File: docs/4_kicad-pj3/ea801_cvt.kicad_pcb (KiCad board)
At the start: 2 copper layers, 4 parts, among them J99 PinHeader_1x02_P2.54mm_Vertic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

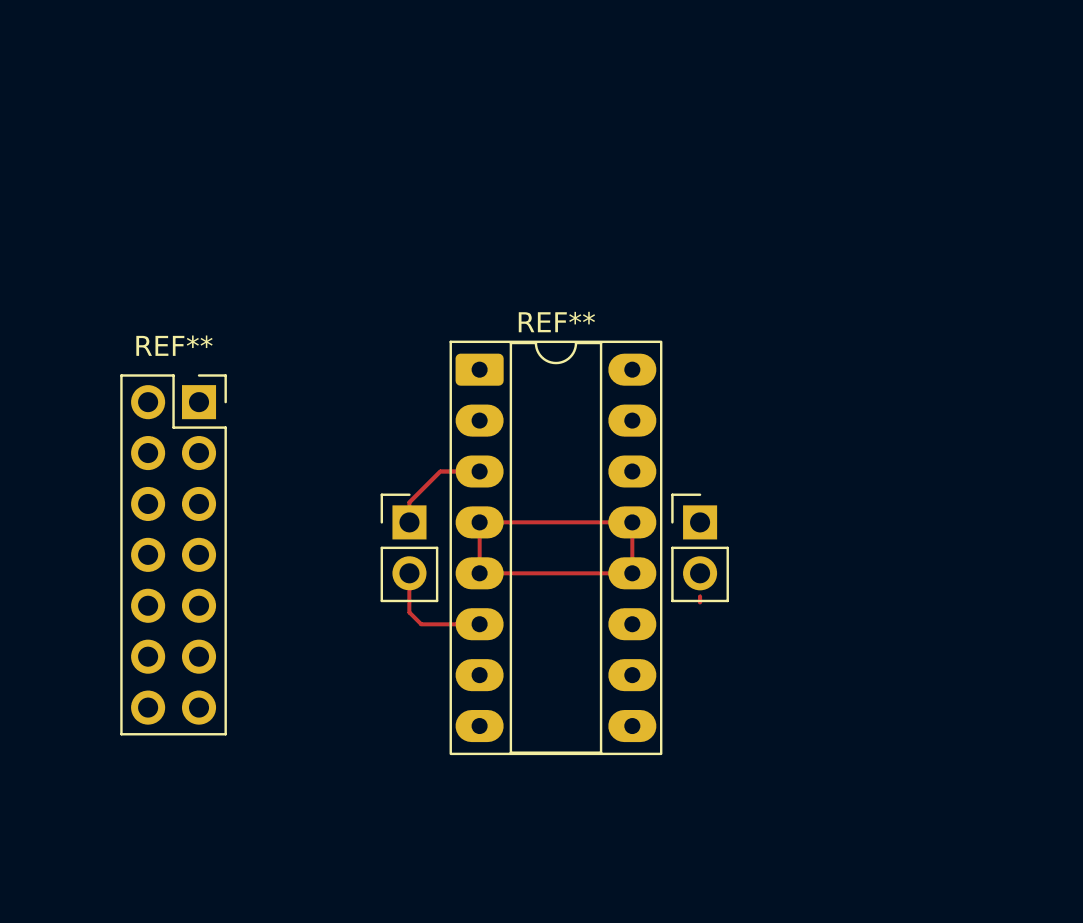
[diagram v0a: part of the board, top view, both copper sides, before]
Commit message: inc imagens, att projeto kicad e att dos arquivos do sensor ToF
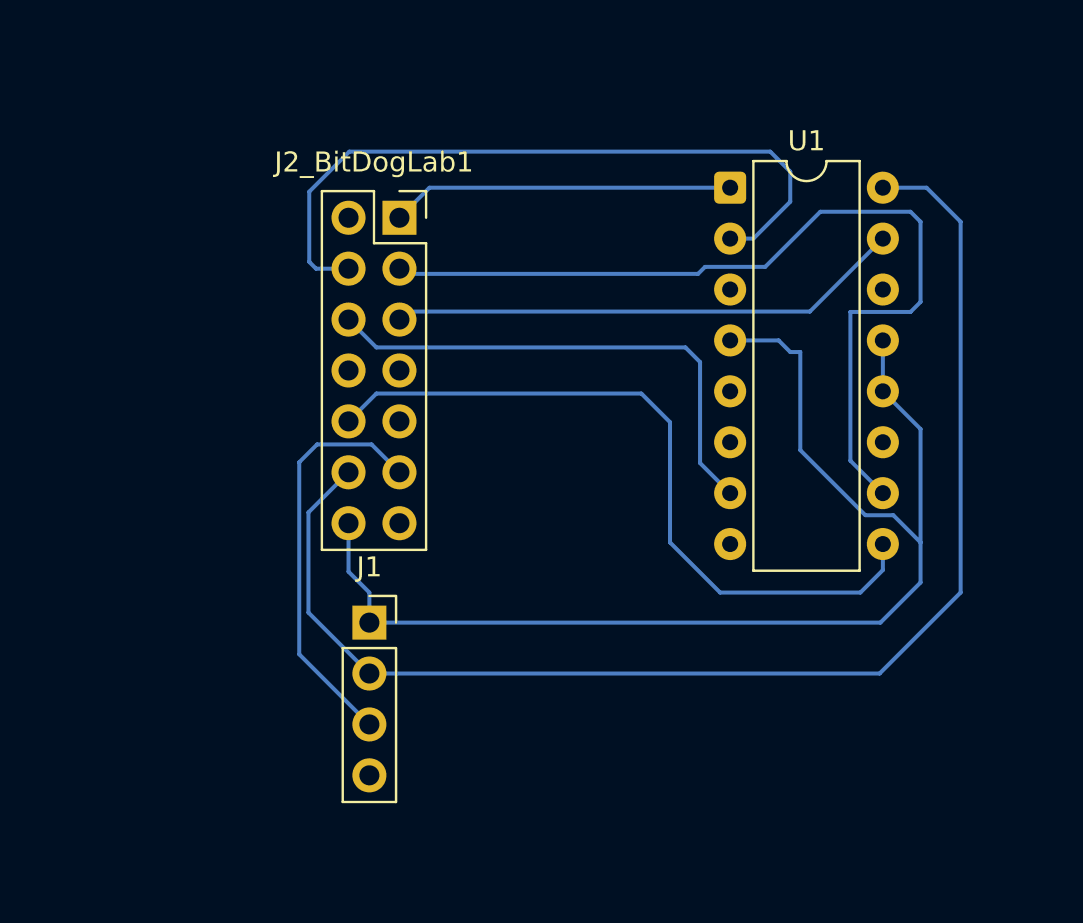
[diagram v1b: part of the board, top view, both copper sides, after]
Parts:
- removed J99, REF**: PinHeader_1x02_P2.54mm_Vertical, Connector_PinHeader_2.54mm:PinHeader_1x02_P2.54mm_Vertical
- removed REF**: CERDIP-16_W7.62mm_SideBrazed_LongPads_Socket, Package_DIP:CERDIP-16_W7.62mm_SideBrazed_LongPads_Socket
- removed REF**: PinSocket_2x07_P2.54mm_Vertical, Connector_PinSocket_2.54mm:PinSocket_2x07_P2.54mm_Vertical
- added J1: Conn_01x04, Connector_PinSocket_2.54mm:PinSocket_1x04_P2.54mm_Vertical, F.Cu at (80.0, 106.0)
- added J2_BitDogLab1: J2_IDC_BitDogLab, Connector_PinSocket_2.54mm:PinSocket_2x07_P2.54mm_Vertical, F.Cu at (81.5, 85.8)
- added U1: L293D, Package_DIP:DIP-16_W7.62mm, F.Cu at (98.0, 84.3)
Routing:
- net /3V3: track 0.00 -> 66.4 mm
- net GND: track 0.00 -> 63.8 mm
- net /GP19: track 0.00 -> 45.6 mm
- net /GP28: track 0.00 -> 36.6 mm
- net /GP16: track 0.00 -> 36.6 mm
- net (no net): track 31.5 -> 0.00 mm
- net /GP20: track 0.00 -> 25.8 mm
- net /GP17: track 0.00 -> 25.6 mm
- net /GP8: track 0.00 -> 20.5 mm
- net Net-(J2_BitDogLab1-Pin_8): track 0.00 -> 17.1 mm
